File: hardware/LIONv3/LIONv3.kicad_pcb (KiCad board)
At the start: 4 copper layers, 45 x 85.1 mm, 83 parts, among them SW1 RESET, SW2 BOOT, U1 TCAN3414DR, U10 INA226AIDGSR, U11 TPS259474ARPWR, U12 XL-1608UGC-04, U13 XL-1608SURC-06, U14 HC-1_25-2PWT, U15 HC-1_25-2PWT, U16 HC-1_25-2PWT, U17 HC-1_25-2PWT, U18 HC-1_25-2PWT, U19 HC-1_25-2PWT, U2 TYPE-C_16PIN_2MD(073), U20 TLV76733DRVR, U21 USBLC6-2SC6, U3 ESP32-C6-MINI-1-N4, U4 TMP112AIDRLR, U5 E80-900M2213S, U6 INA226AIDGSR, U7 XL-1608UBC-04, U8 W25Q16JVSSIQTR, U9 HC-1_25-2PWT

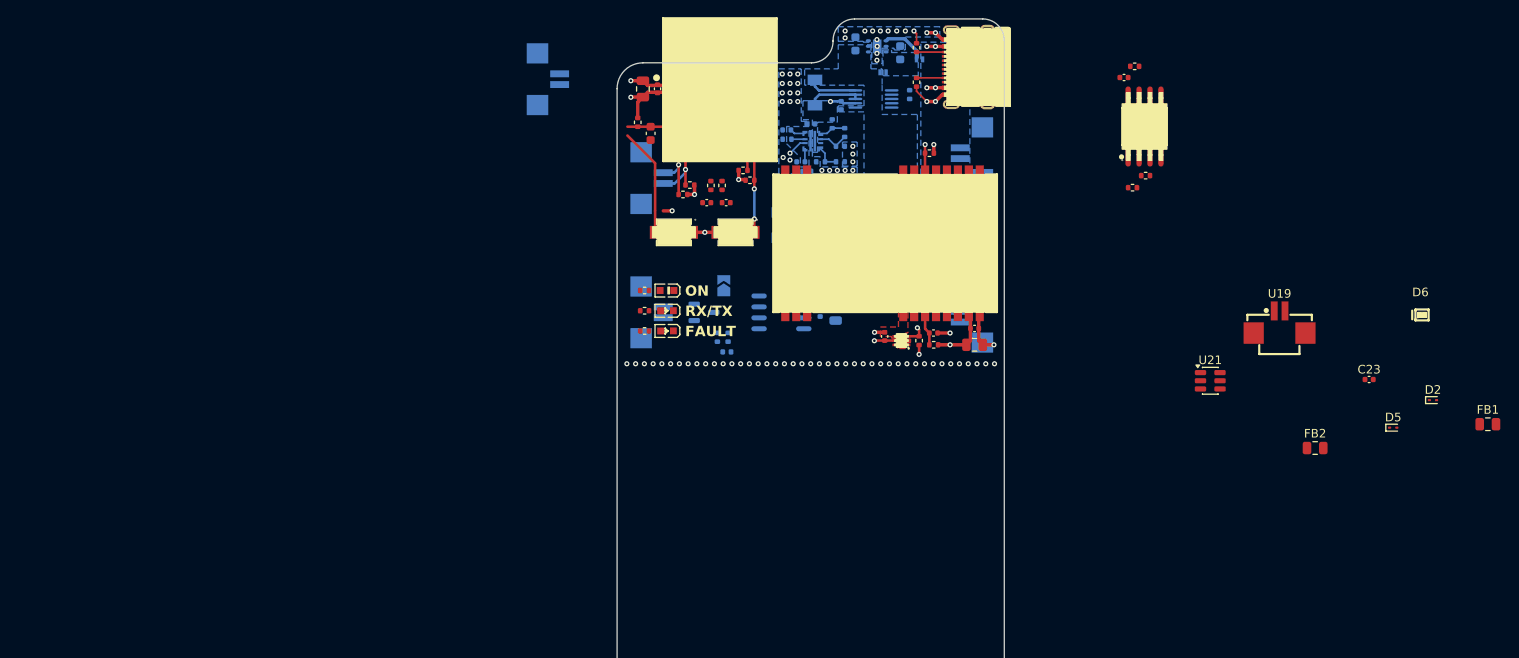
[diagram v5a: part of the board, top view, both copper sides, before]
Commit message: feat(hardware): add TestPoints
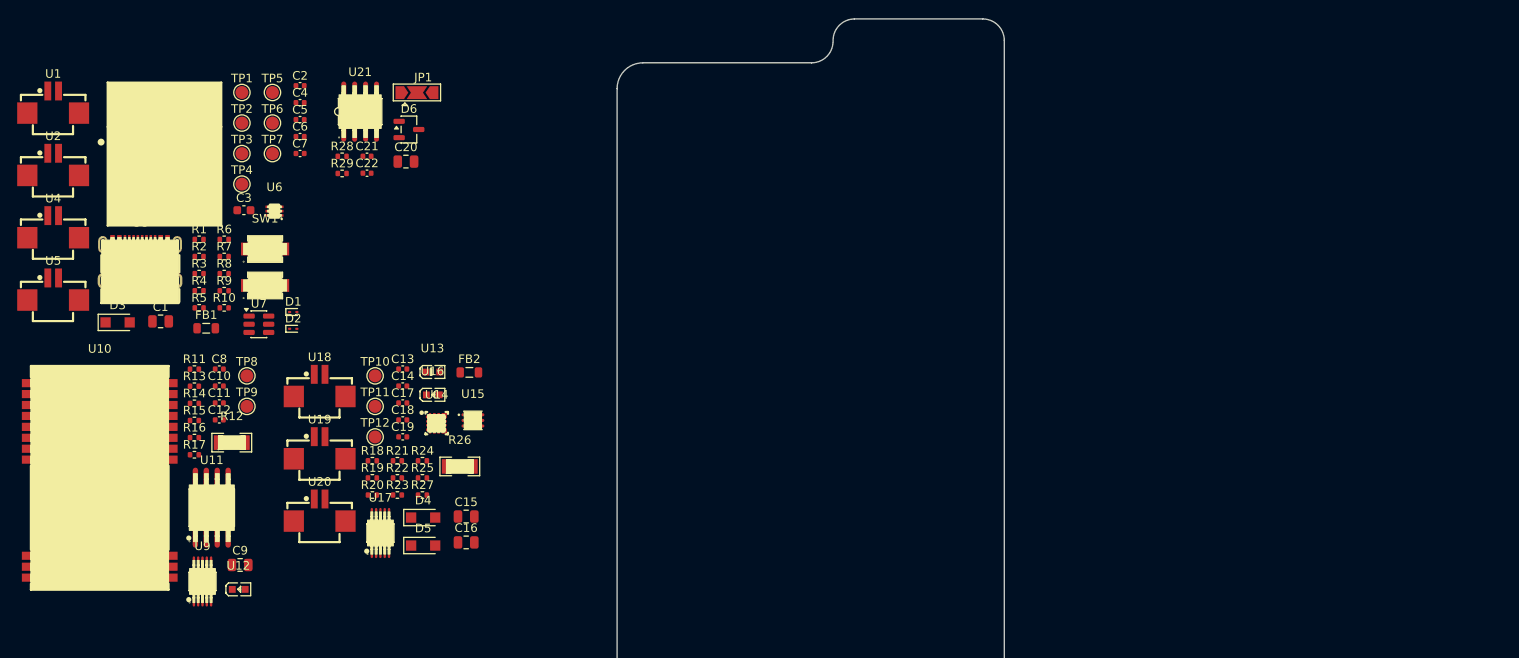
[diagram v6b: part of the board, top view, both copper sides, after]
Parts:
- removed C23: 100nF, Capacitor_SMD:C_0402_1005Metric
- removed R32: 34.8k, Resistor_SMD:R_0402_1005Metric
- added C3: 1uF, Capacitor_SMD:C_0603_1608Metric, F.Cu at (114.6, 80.6)
- added R1: 10k, Resistor_SMD:R_0402_1005Metric, F.Cu at (109.4, 84.0)
- added TP1: TestPoint_Square, TestPoint:TestPoint_Pad_D1.5mm, F.Cu at (114.4, 66.9)
- added TP10: TestPoint_Square, TestPoint:TestPoint_Pad_D1.5mm, F.Cu at (129.9, 99.9)
- added TP11: TestPoint_Square, TestPoint:TestPoint_Pad_D1.5mm, F.Cu at (129.9, 103.4)
- added TP12: TestPoint_Square, TestPoint:TestPoint_Pad_D1.5mm, F.Cu at (129.9, 107.0)
- added TP2: TestPoint_Square, TestPoint:TestPoint_Pad_D1.5mm, F.Cu at (114.4, 70.5)
- added TP3: TestPoint_Square, TestPoint:TestPoint_Pad_D1.5mm, F.Cu at (114.4, 74.0)
- added TP4: TestPoint_Square, TestPoint:TestPoint_Pad_D1.5mm, F.Cu at (114.4, 77.6)
- added TP5: TestPoint_Square, TestPoint:TestPoint_Pad_D1.5mm, F.Cu at (117.9, 66.9)
- added TP6: TestPoint_Square, TestPoint:TestPoint_Pad_D1.5mm, F.Cu at (117.9, 70.5)
- added TP7: TestPoint_Square, TestPoint:TestPoint_Pad_D1.5mm, F.Cu at (117.9, 74.0)
- added TP8: TestPoint_Square, TestPoint:TestPoint_Pad_D1.5mm, F.Cu at (115.0, 99.9)
- added TP9: TestPoint_Square, TestPoint:TestPoint_Pad_D1.5mm, F.Cu at (115.0, 103.4)
- C1: value 10uF -> 22uF; moved to F.Cu
- C12, C2, R12, U18: moved to F.Cu
- C13: value 100nF -> 1uF
- C14: value TBD -> 1uF
- C15: value TBD -> 22uF; footprint Capacitor_SMD:C_0402_1005Metric -> Capacitor_SMD:C_0805_2012Metric
- C16: value 100nF -> 22uF; footprint Capacitor_SMD:C_0402_1005Metric -> Capacitor_SMD:C_0805_2012Metric; moved to F.Cu
- C17: value 1uF -> 3.3nF; moved to F.Cu
- C18: value 3.3nF -> 2.2nF; moved to F.Cu
- C19: value 2.2nF -> 100nF; moved to F.Cu
- C20: value 1uF -> 10uF; footprint Capacitor_SMD:C_0402_1005Metric -> Capacitor_SMD:C_0805_2012Metric; moved to F.Cu
- C21: value 2.2uF -> 100nF; footprint Capacitor_SMD:C_0603_1608Metric -> Capacitor_SMD:C_0402_1005Metric; moved to F.Cu
- C22: value 2.2uF -> 4.7nF; footprint Capacitor_SMD:C_0603_1608Metric -> Capacitor_SMD:C_0402_1005Metric; moved to F.Cu
- C4: value 1uF -> 100nF; footprint Capacitor_SMD:C_0603_1608Metric -> Capacitor_SMD:C_0402_1005Metric
- C5: value 22uF -> DNP; footprint Capacitor_SMD:C_0805_2012Metric -> Capacitor_SMD:C_0402_1005Metric
- C6: value 4.7nF -> DNP; moved to F.Cu
- D1: value TI ESD752DBZR -> ESD9B3.3ST5G; footprint Package_TO_SOT_SMD:SOT-23-3 -> Diode_SMD:D_SOD-923; moved to F.Cu
- D3, D4: value D_Schottky -> PMEG2010ER; footprint LIONv3-Footprints:X2-DFN1006-2_L1.0-W0.6-P0.65-RD -> Diode_SMD:Nexperia_CFP3_SOD-123W; moved to F.Cu
- D5: value ESD9B3.3ST5G -> PMEG2010ER; footprint Diode_SMD:D_SOD-923 -> Diode_SMD:Nexperia_CFP3_SOD-123W
- D6: value D_Schottky -> TI ESD752DBZR; footprint LIONv3-Footprints:X2-DFN1006-2_L1.0-W0.6-P0.65-RD -> Package_TO_SOT_SMD:SOT-23-3
- FB1, FB2: value 220Ω@100MHz -> BLM21PG221SN1D; footprint Capacitor_SMD:C_0805_2012Metric -> Inductor_SMD:L_0805_2012Metric
- JP1: value Jumper_2_Open -> SolderJumper_3_Open; footprint Jumper:SolderJumper-2_P1.3mm_Open_TrianglePad1.0x1.5mm -> Jumper:SolderJumper-3_P2.0mm_Open_TrianglePad1.0x1.5mm; moved to F.Cu
- R10: value 10k -> 5.1k
- R14: value 1k -> 10k
- R17, R20: value 10k -> 120; moved to F.Cu
- R18: value 50m -> 60.4k; footprint LIONv3-Footprints:R1206 -> Resistor_SMD:R_0402_1005Metric; moved to F.Cu
- R19: value 60.4k -> 15k; moved to F.Cu
- R2, R3: value 59 -> 4.7k; moved to F.Cu
- R21: value 3.32k -> 10k; moved to F.Cu
- R22: value 15k -> 10k; moved to F.Cu
- R23: value 10k -> 34.8k; moved to F.Cu
- R24: value 2.2k -> 430
- R25: value 1k -> 3.32k
- R26: value 4.7k -> 50m; footprint Resistor_SMD:R_0402_1005Metric -> LIONv3-Footprints:R1206
- R27: value 4.7k -> 10k
- R28, R29: value 0 -> 59
- R5: value 5.1k -> 10k
- R6: value 5.1k -> 0
- R7: value 10k -> 4.7k
- R8: value 10k -> 0
- R9: value 4.7k -> 5.1k
- U1: value TCAN3414DR -> HC-1_25-2PWT; footprint LIONv3-Footprints:SOIC-8_L4.9-W3.9-P1.27-LS6.0-BL -> LIONv3-Footprints:CONN-SMD_2P-P1.25-HC-1.25-2PWT; moved to F.Cu
- U10: value INA226AIDGSR -> E80-900M2213S; footprint LIONv3-Footprints:MSOP-10_L3.0-W3.0-P0.50-LS5.0-BL -> LIONv3-Footprints:WIFIM-SMD_22P-L26.0-W16.0-P1.27-TL; moved to F.Cu
- U11: value TPS259474ARPWR -> W25Q16JVSSIQTR; footprint LIONv3-Footprints:VQFN-10_L2.0-W2.0-P0.45-TL -> LIONv3-Footprints:SOIC-8_L5.3-W5.3-P1.27-LS8.0-BL; moved to F.Cu
- U12: value XL-1608UGC-04 -> XL-1608UBC-04; footprint LIONv3-Footprints:LED0603-RD_GREEN -> LIONv3-Footprints:LED0603-RD_BLUE
- U13: value XL-1608SURC-06 -> XL-1608UGC-04; footprint LIONv3-Footprints:LED0603-RD_RED -> LIONv3-Footprints:LED0603-RD_GREEN
- U14: value HC-1_25-2PWT -> TPS259474ARPWR; footprint LIONv3-Footprints:CONN-SMD_2P-P1.25-HC-1.25-2PWT -> LIONv3-Footprints:VQFN-10_L2.0-W2.0-P0.45-TL; moved to F.Cu
- U15: value HC-1_25-2PWT -> TLV76733DRVR; footprint LIONv3-Footprints:CONN-SMD_2P-P1.25-HC-1.25-2PWT -> LIONv3-Footprints:WSON-6_L2.0-W2.0-P0.65-TL-EP; moved to F.Cu
- U16: value HC-1_25-2PWT -> XL-1608SURC-06; footprint LIONv3-Footprints:CONN-SMD_2P-P1.25-HC-1.25-2PWT -> LIONv3-Footprints:LED0603-RD_RED; moved to F.Cu
- U17, U9: value HC-1_25-2PWT -> INA226AIDGSR; footprint LIONv3-Footprints:CONN-SMD_2P-P1.25-HC-1.25-2PWT -> LIONv3-Footprints:MSOP-10_L3.0-W3.0-P0.50-LS5.0-BL; moved to F.Cu
- U2: value TYPE-C_16PIN_2MD(073) -> HC-1_25-2PWT; footprint LIONv3-Footprints:USB-C-SMD_TYPE-C-16PIN-2MD-073 -> LIONv3-Footprints:CONN-SMD_2P-P1.25-HC-1.25-2PWT
- U20: value TLV76733DRVR -> HC-1_25-2PWT; footprint LIONv3-Footprints:WSON-6_L2.0-W2.0-P0.65-TL-EP -> LIONv3-Footprints:CONN-SMD_2P-P1.25-HC-1.25-2PWT; moved to F.Cu
- U21: value USBLC6-2SC6 -> TCAN3414DR; footprint Package_TO_SOT_SMD:SOT-23-6 -> LIONv3-Footprints:SOIC-8_L4.9-W3.9-P1.27-LS6.0-BL
- U4: value TMP112AIDRLR -> HC-1_25-2PWT; footprint LIONv3-Footprints:SOT-563_L1.6-W1.2-P0.50-LS1.6-BR -> LIONv3-Footprints:CONN-SMD_2P-P1.25-HC-1.25-2PWT
- U5: value E80-900M2213S -> HC-1_25-2PWT; footprint LIONv3-Footprints:WIFIM-SMD_22P-L26.0-W16.0-P1.27-TL -> LIONv3-Footprints:CONN-SMD_2P-P1.25-HC-1.25-2PWT
- U6: value INA226AIDGSR -> TMP112AIDRLR; footprint LIONv3-Footprints:MSOP-10_L3.0-W3.0-P0.50-LS5.0-BL -> LIONv3-Footprints:SOT-563_L1.6-W1.2-P0.50-LS1.6-BR; moved to F.Cu
- U7: value XL-1608UBC-04 -> USBLC6-2SC6; footprint LIONv3-Footprints:LED0603-RD_BLUE -> Package_TO_SOT_SMD:SOT-23-6
- U8: value W25Q16JVSSIQTR -> TYPE-C_16PIN_2MD(073); footprint LIONv3-Footprints:SOIC-8_L5.3-W5.3-P1.27-LS8.0-BL -> LIONv3-Footprints:USB-C-SMD_TYPE-C-16PIN-2MD-073
- moved FB1 149.4 mm to (110.2, 94.3)
- moved D2 132.7 mm to (120.4, 94.4)
- moved D6 119.7 mm to (133.8, 71.2)
- moved U8 117.8 mm to (102.6, 86.4)
- moved R15 116.8 mm to (108.9, 105.1)
- moved R16 114.7 mm to (108.9, 107.1)
- moved D5 113.6 mm to (135.5, 119.6)
- moved U19 112.5 mm to (123.4, 108.2)
- moved R13 111.4 mm to (108.9, 101.1), turned to 0 degrees
- moved U2 106.8 mm to (92.5, 75.3), turned to 0 degrees
- moved U21 103.6 mm to (128.1, 69.2)
- moved U10 100.3 mm to (97.9, 112.0), turned to 0 degrees
- moved U4 99.5 mm to (92.5, 82.5)
- moved FB2 98.7 mm to (140.8, 99.5)
- moved D3 98.1 mm to (100.0, 93.7)
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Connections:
- C10 pad 1: 3.3V_RF -> +3.3V
- C11 pad 1: /LR_RST -> +3.3V
- C12 pad 1: +3.3V -> /LR_RST
- C14 pad 1: /USB_D+ -> +3.3V_eFuse
- C15 pad 1: /USB_D- -> +4.69V
- C16 pad 1: /POWER/PWR -> +3.3V_LDO
- C17 pad 1: /POWER/3V3_IN -> Net-(U14-ITIMER)
- C18 pad 1: Net-(U11-ITIMER) -> Net-(U14-DVDT)
- C19 pad 1: Net-(U11-DVDT) -> +3.3V_LDO
- C21 pad 1: +5V -> +3.3V
- C22 pad 1: /POWER/PWR -> GND
- C22 pad 2: GND -> Net-(JP1-C)
- C4 pad 1: Net-(D2-A2) -> +3.3V
- C5 pad 1: +3.3V -> /USB_D+
- C6 pad 1: Net-(C6-Pad1) -> /USB_D-
- C7 pad 1: +3.3V -> +4.69V
- C8 pad 1: +3.3V -> 3.3V_RF
- D1 pad 1: /CAN_A_N -> GND
- D1 pad 2: /CAN_A_P -> Net-(D1-A2)
- D2 pad 2: Net-(D2-A2) -> /IO9
- D3 pad 1: +5V -> +4.69V
- D4 pad 1: +5V -> +4.69V
- D4 pad 2: /POWER/PWR -> +3.3V_LDO
- D5 pad 1: GND -> +4.69V
- D5 pad 2: /IO9 -> Net-(D5-A)
- D6 pad 1: +5V -> /CAN_N
- D6 pad 2: Net-(D6-A) -> /CAN_P
- FB1 pad 1: Net-(D6-A) -> Net-(D3-A)
- FB2 pad 1: Net-(D3-A) -> Net-(D5-A)
- JP1 pad 1: /CAN_A_P -> Net-(JP1-A)
- JP1 pad 2: Net-(JP1-B) -> Net-(JP1-C)
- R10 pad 1: 3.3V_RF -> Net-(U8-CC2)
- R10 pad 2: /LR_NSS -> GND
- R11 pad 2: /LR_RST -> /LR_CS#
- R13 pad 2: /FLASH_CS -> /FLASH_CS#
- R14 pad 1: Net-(U7-A) -> 3.3V_RF
- R14 pad 2: /LR_LED -> /LR_RST
- R15 pad 2: Net-(U8-IO3) -> Net-(U11-IO3)
- R16 pad 2: Net-(U8-IO2) -> Net-(U11-IO2)
- R17 pad 1: /INA_ALERT -> Net-(U12-A)
- R17 pad 2: /POWER/PWR -> /LR_LED
- R18 pad 1: /POWER/PWR -> +3.3V_eFuse
- R18 pad 2: /POWER/3V3_IN -> Net-(U14-EN/UVLO)
- R19 pad 1: /POWER/3V3_IN -> +3.3V
- R19 pad 2: Net-(U11-EN/UVLO) -> Net-(U14-FLT#/PGTH)
- R2 pad 1: Net-(JP1-B) -> +3.3V
- R2 pad 2: Net-(C6-Pad1) -> /I2C_SDA
- R20 pad 1: Net-(U11-EN/UVLO) -> Net-(U13-A)
- R20 pad 2: Net-(U11-OVLO/OVCSEL) -> +3.3V
- R21 pad 1: Net-(U11-ILM) -> Net-(U14-EN/UVLO)
- R21 pad 2: GND -> Net-(U14-OVLO/OVCSEL)
- R22 pad 1: +3.3V -> Net-(U14-FLT#/PGTH)
- R22 pad 2: Net-(U11-FLT#/PGTH) -> GND
- R23 pad 1: Net-(U11-FLT#/PGTH) -> Net-(U14-OVLO/OVCSEL)
- R24 pad 1: Net-(U12-A) -> Net-(U16-A)
- R24 pad 2: +3.3V -> +3.3V_eFuse
- R25 pad 1: Net-(U13-A) -> Net-(U14-ILM)
- R25 pad 2: /POWER/3V3_IN -> GND
- R26 pad 1: /I2C_SCL -> +3.3V_LDO
- R26 pad 2: +3.3V -> +3.3V_eFuse
- R27 pad 1: +3.3V -> /INA_ALERT
- R27 pad 2: /I2C_SDA -> +3.3V_LDO
- R28 pad 1: Net-(U3-IO13) -> /CAN_P
- R28 pad 2: /USB_D+ -> Net-(JP1-A)
- R29 pad 1: Net-(U3-IO12) -> Net-(JP1-B)
- R29 pad 2: /USB_D- -> /CAN_N
- R3 pad 1: Net-(C6-Pad1) -> /I2C_SCL
- R3 pad 2: /CAN_A_N -> +3.3V
- R4 pad 2: Net-(D2-A2) -> /IO9
- R5 pad 1: Net-(U2-CC1) -> +3.3V
- R5 pad 2: GND -> /IO8
- R6 pad 1: Net-(U2-CC2) -> Net-(U3-IO13)
- R6 pad 2: GND -> /USB_D+
- R7 pad 2: /IO9 -> /TMP_ALERT
- R8 pad 1: +3.3V -> Net-(U3-IO12)
- R8 pad 2: /IO8 -> /USB_D-
- R9 pad 1: +3.3V -> Net-(U8-CC1)
- R9 pad 2: /TMP_ALERT -> GND
- SW1 pad 2: Net-(D2-A2) -> Net-(D1-A2)
- U1 pad 1: /CAN_TX -> /CAN_N
- U1 pad 2: GND -> /CAN_P
- U1 pad 3: +3.3V -> GND
- U1 pad 4: /CAN_RX -> GND
- U10 pad 2: /I2C_SDA -> unconnected-(U10-NC-Pad2)
- U10 pad 3: /INA_ALERT -> /SPI_POCI
- U10 pad 4: /I2C_SDA -> /SPI_PICO
- U10 pad 5: /I2C_SCL -> /SPI_SCK
- U10 pad 6: /POWER/PWR -> /LR_CS#
- U10 pad 7: GND -> /LR_BUSY
- U10 pad 8: /POWER/3V3_IN -> GND
- U11 pad 1: Net-(U11-EN/UVLO) -> /FLASH_CS#
- U11 pad 2: Net-(U11-OVLO/OVCSEL) -> /SPI_POCI
- U11 pad 3: /POWER/LED_FAULT -> Net-(U11-IO2)
- U11 pad 4: Net-(U11-FLT#/PGTH) -> GND
- U11 pad 5: /POWER/3V3_IN -> /SPI_PICO
- U11 pad 6: +3.3V -> /SPI_SCK
- U11 pad 7: Net-(U11-DVDT) -> Net-(U11-IO3)
- U11 pad 8: GND -> +3.3V
- U13 pad 1: /POWER/LED_FAULT -> GND
- U14 pad 1: /CAN_A_N -> Net-(U14-EN/UVLO)
- U14 pad 2: /CAN_A_P -> Net-(U14-OVLO/OVCSEL)
- U14 pad 3: GND -> /POWER/LED_FAULT
- U14 pad 4: GND -> Net-(U14-FLT#/PGTH)
- U15 pad 1: /I2C_SCL -> +3.3V_LDO
- U15 pad 2: /I2C_SDA -> +3.3V_LDO
- U15 pad 4: GND -> +4.69V
- U16 pad 1: /POWER/PWR -> /POWER/LED_FAULT
- U16 pad 2: /POWER/PWR -> Net-(U16-A)
- U17 pad 1: Net-(FB2-Pad2) -> GND
- U17 pad 2: Net-(FB2-Pad2) -> /I2C_SDA
- U17 pad 3: GND -> /INA_ALERT
- U17 pad 4: GND -> /I2C_SDA
- U18 pad 1: GND -> Net-(FB2-Pad2)
- U18 pad 2: GND -> Net-(FB2-Pad2)
- U19 pad 1: /CAN_A_N -> +3.3V_LDO
- U19 pad 2: /CAN_A_P -> +3.3V_LDO
- U20 pad 1: /POWER/PWR -> GND
- U20 pad 2: /POWER/PWR -> GND
- U20 pad 4: +5V -> GND
- U21 pad 1: /D- -> /CAN_TX
- U21 pad 3: /D+ -> +3.3V
- U21 pad 4: /USB_D+ -> /CAN_RX
- U21 pad 5: +5V -> GND
- U21 pad 6: /USB_D- -> /CAN_N
- U3 pad 16: /SPI_MOSI -> /SPI_PICO
- U3 pad 24: /LR_NSS -> /LR_CS#
- U3 pad 30: /UART_RX0 -> /UART_RX
- U3 pad 31: /UART_TX0 -> /UART_TX
- U3 pad 5: /SPI_MISO -> /SPI_POCI
- U3 pad 8: Net-(D2-A2) -> Net-(D1-A2)
- U3 pad 9: /FLASH_CS -> /FLASH_CS#
- U4 pad 1: /I2C_SCL -> /CAN_N
- U4 pad 2: GND -> /CAN_P
- U4 pad 3: /TMP_ALERT -> GND
- U5 pad 1: GND -> /I2C_SCL
- U5 pad 2: unconnected-(U5-NC-Pad2) -> /I2C_SDA
- U5 pad 3: /SPI_MISO -> GND
- U5 pad 4: /SPI_MOSI -> GND
- U6 pad 1: GND -> /I2C_SCL
- U6 pad 3: unconnected-(U6-Alert-Pad3) -> /TMP_ALERT
- U6 pad 4: /I2C_SDA -> GND
- U6 pad 5: /I2C_SCL -> +3.3V
- U6 pad 6: +3.3V -> /I2C_SDA
- U7 pad 1: GND -> Net-(U8-Dp1)
- U7 pad 2: Net-(U7-A) -> GND
- U9 pad 1: /UART_TX0 -> GND
- U9 pad 2: /UART_RX0 -> GND
- U9 pad 3: GND -> unconnected-(U9-Alert-Pad3)
- U9 pad 4: GND -> /I2C_SDA
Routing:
- net GND: track 36.8 -> 0.00 mm, vias 124 -> 0
- net Net-(D2-A2): track 17.4 -> 0.00 mm
- net +3.3V: track 14.7 -> 0.00 mm, vias 15 -> 0
- net /IO9: track 9.00 -> 0.00 mm, vias 2 -> 0
- net 3.3V_RF: track 8.36 -> 0.00 mm, vias 2 -> 0
- net /I2C_SDA: track 7.00 -> 0.00 mm, vias 1 -> 0
- net /I2C_SCL: track 6.96 -> 0.00 mm, vias 1 -> 0
- net /POWER/3V3_IN: track 6.13 -> 0.00 mm
- net /POWER/PWR: track 5.66 -> 0.00 mm
- net +5V: track 5.22 -> 0.00 mm
- net Net-(FB1-Pad2): track 4.60 -> 0.00 mm, vias 4 -> 0
- net /LR_RST: track 4.00 -> 0.00 mm
- net Net-(U11-OVLO/OVCSEL): track 3.63 -> 0.00 mm
- net Net-(U2-CC2): track 3.50 -> 0.00 mm
- net Net-(U2-CC1): track 3.50 -> 0.00 mm
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- removed copper zone on B.Cu, net +3.3V
- removed copper zone on In2.Cu, net +3.3V
- removed copper zone on B.Cu, net +5V
- removed copper zone on B.Cu, net /POWER/3V3_IN
- removed copper zone on B.Cu, net /POWER/PWR
- removed copper zone on B.Cu, net GND
- removed copper zone on F.Cu, net GND
- removed copper zone on In1.Cu, net GND
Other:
- board text removed: "FAULT"
- board text removed: "ON"
- board text removed: "RX/TX"

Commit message: feat(hardware): start PCB design
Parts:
- C13, C14: footprint Capacitor_SMD:C_0402_1005Metric -> Capacitor_SMD:C_0603_1608Metric
- D3, FB1: moved to B.Cu
- U3: footprint LIONv3-Footprints:WIFIM-SMD_61P-L16.6-W13.2-P0.80-ESP32-C6-MINI-1-N4 -> RF_Module:ESP32-C6-MINI-1
- moved TP7 195.9 mm to (-53.0, 169.7)
- moved U19 171.0 mm to (-47.3, 98.1)
- moved U20 171.0 mm to (-47.3, 105.4)
- moved FB2 167.0 mm to (-24.9, 79.0), turned to 180 degrees
- moved TP9 166.2 mm to (269.7, 42.6), turned to 180 degrees
- moved D5 166.0 mm to (-24.9, 76.8)
- moved TP8 163.8 mm to (269.7, 46.2), turned to 180 degrees
- moved U18 149.5 mm to (-24.9, 82.7)
- moved U9 149.1 mm to (251.5, 77.4), turned to -90 degrees
- moved R12 147.3 mm to (257.3, 76.6), turned to -90 degrees
- moved C11 145.7 mm to (255.4, 78.1), turned to 90 degrees
- moved U1 143.0 mm to (-48.3, 43.1)
- moved U2 143.0 mm to (-48.3, 50.3)
- moved U4 143.0 mm to (-48.3, 57.6)
- moved U5 143.0 mm to (-48.3, 64.8)
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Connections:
- net Net-(U8-Dn1) renamed /D-
- net Net-(U8-Dp1) renamed /D+
- D6 pad 1: /CAN_N -> /CAN_P
- D6 pad 2: /CAN_P -> /CAN_N
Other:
- board size 45 x 85.1 mm -> 50.4 x 85 mm

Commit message: feat(hardware): add board form-factor
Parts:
- removed U4: HC-1_25-2PWT, LIONv3-Footprints:CONN-SMD_2P-P1.25-HC-1.25-2PWT
- added H1: MountingHole_Pad, MountingHole:MountingHole_2.5mm_Pad, F.Cu at (116.6, 79.1)
- added H2: MountingHole_Pad, MountingHole:MountingHole_2.5mm_Pad, F.Cu at (116.6, 114.2)
- added H3: MountingHole_Pad, MountingHole:MountingHole_2.5mm_Pad, F.Cu at (71.5, 114.2)
- C11, C13, C14, C15, C16, C17, C18, C19, C20, C21, C22, D4, D5, D6, FB2, JP1, R12, R18, R19, R21, R22, R23, R25, R26, R27, R28, R29, TP1, TP10, TP11, TP12, TP2, TP3, TP4, TP5, TP6, TP7, TP8, TP9, U1, U14, U15, U17, U18, U19, U2, U20, U21, U5, U9: moved to B.Cu
- moved U1 175.6 mm to (115.7, 105.9), turned to -90 degrees
- moved U19 163.0 mm to (115.7, 96.4), turned to -90 degrees
- moved C20 161.8 mm to (91.8, 106.0)
- moved U20 161.0 mm to (111.7, 80.0)
- moved R12 158.7 mm to (100.1, 98.9)
- moved C21 158.3 mm to (93.6, 106.0)
- moved C11 155.0 mm to (102.0, 100.5)
- moved U21 149.5 mm to (98.0, 106.0)
- moved U9 147.3 mm to (105.9, 99.7)
- moved R13 140.7 mm to (104.1, 90.9)
- moved R15 140.7 mm to (91.8, 89.6)
- moved R16 140.7 mm to (104.1, 88.3)
- moved U11 140.7 mm to (97.9, 89.0)
- moved C10 140.7 mm to (92.3, 91.4)
- moved U18 140.7 mm to (115.7, 87.0), turned to -90 degrees
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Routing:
- net GND: vias 0 -> 296
- added copper zone on F.Cu, net GND
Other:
- board size 50.4 x 85 mm -> 51 x 86 mm
